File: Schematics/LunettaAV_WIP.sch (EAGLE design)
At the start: 98 parts, among them IC1 TLC339P, IC10 40106N, IC2 4046N, IC3 7809\, IC4 4040N, IC5 7805, IC6 4017N, IC7 4051N, IC8 4094N, J1 POWER_JACKPOWER_JACK_SLOT, U1 LM358, U3 LM358

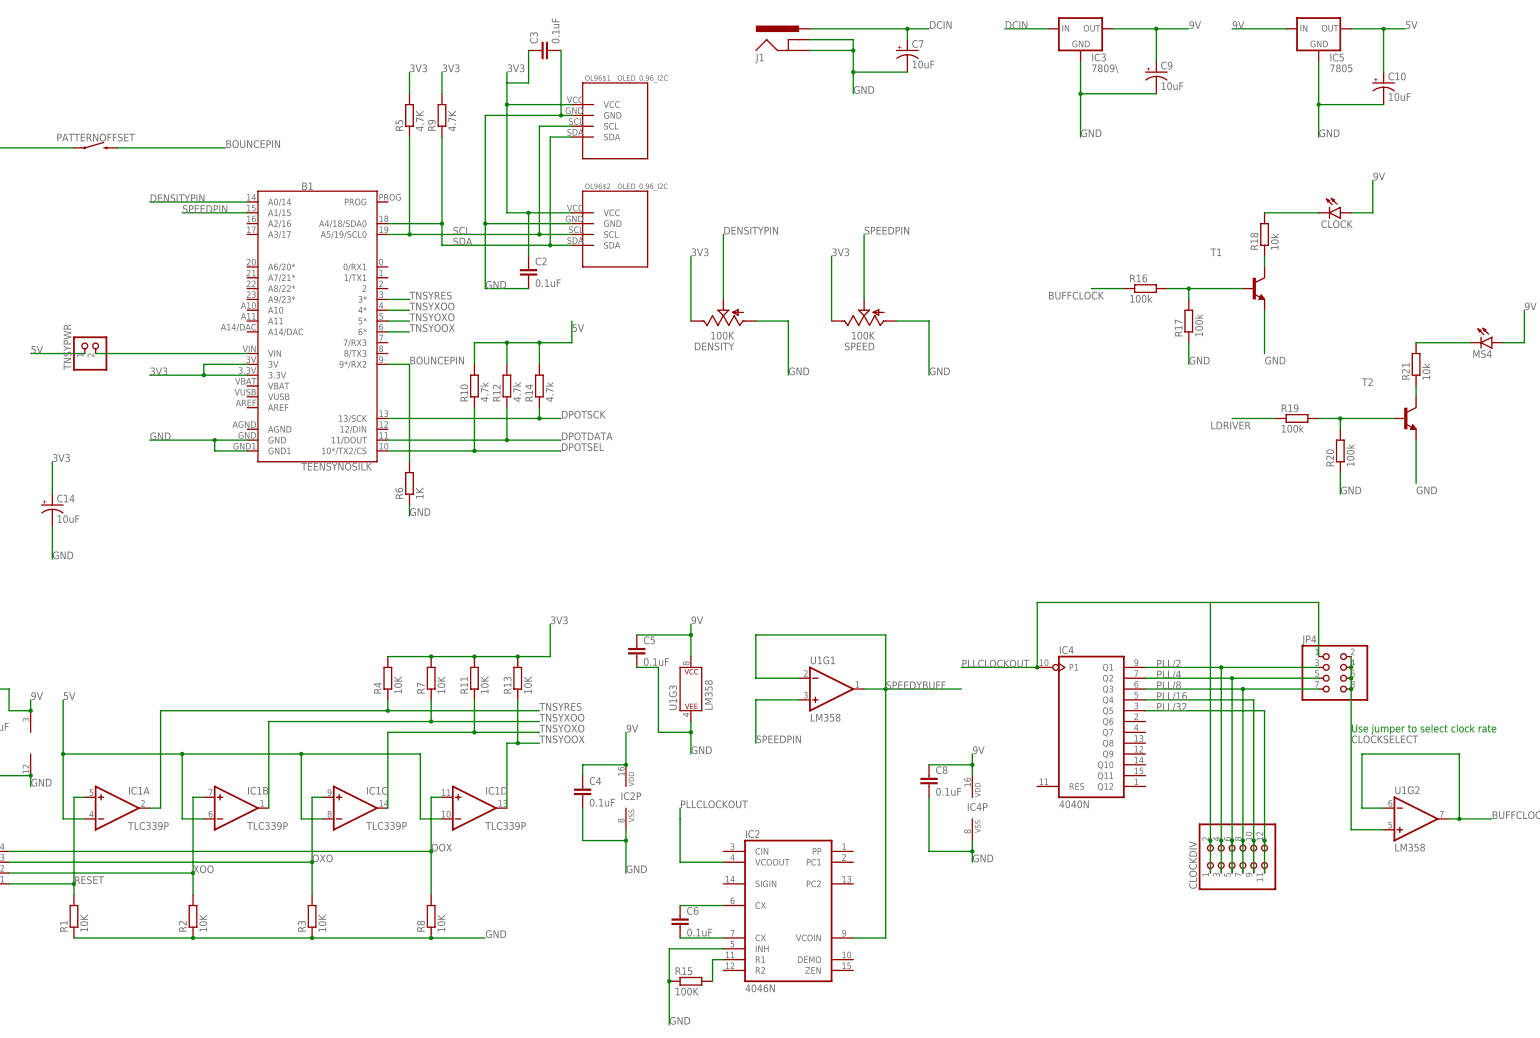
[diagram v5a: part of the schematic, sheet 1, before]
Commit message: fix minor schematic issues for a cleaner bom
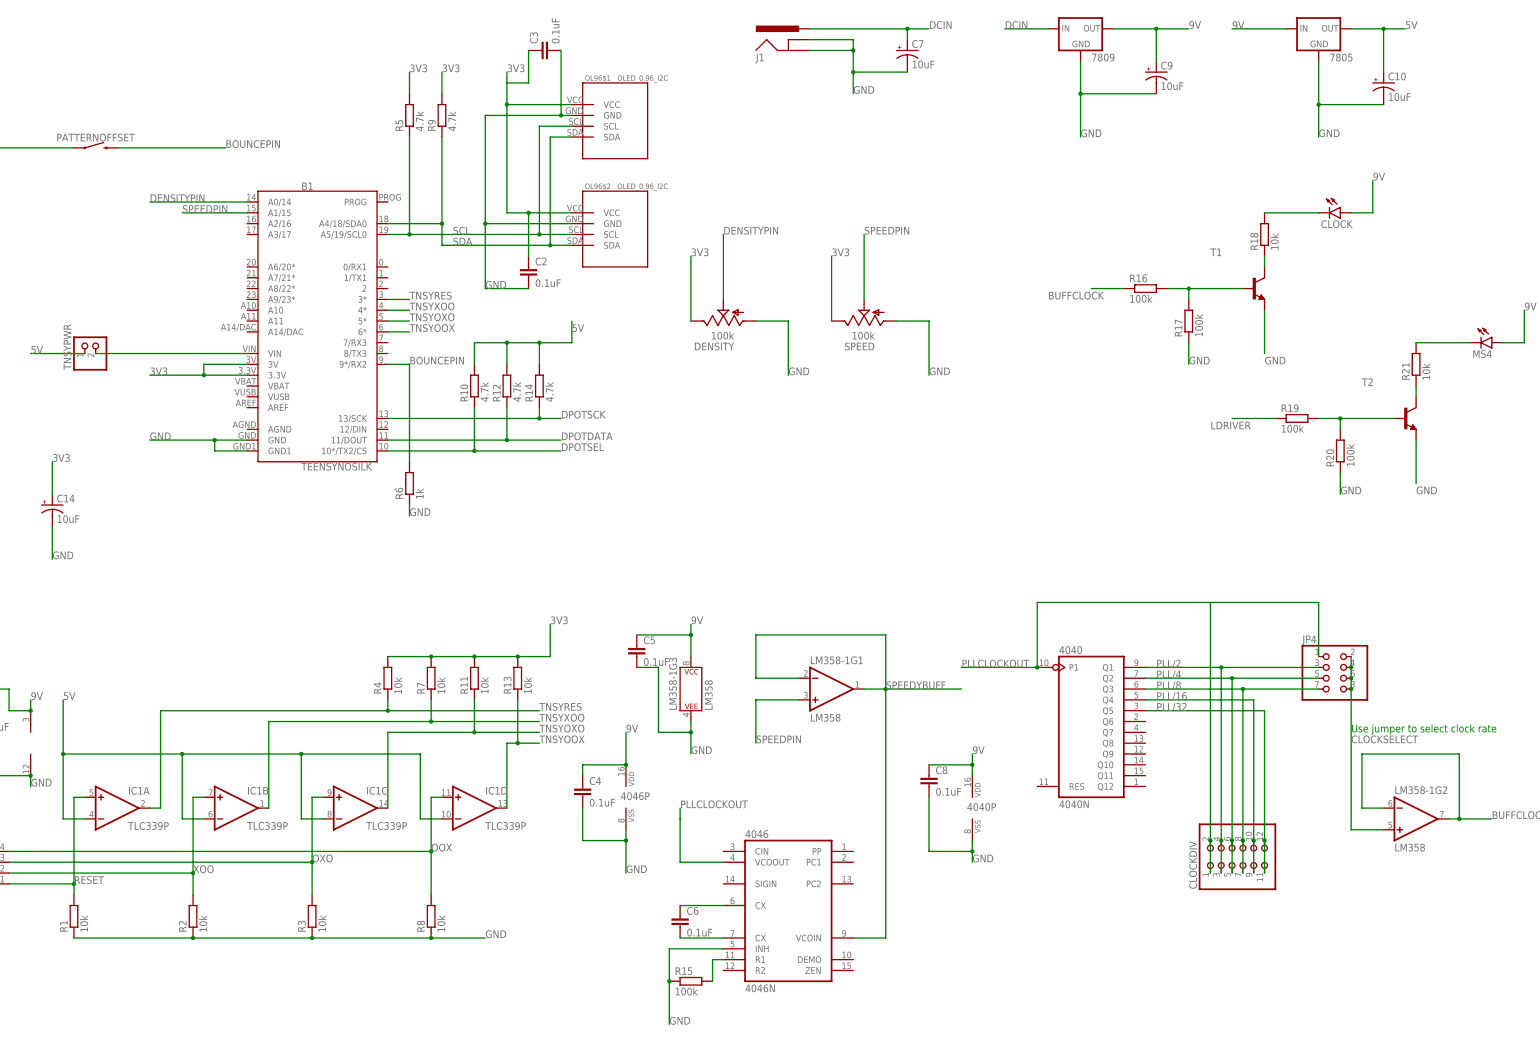
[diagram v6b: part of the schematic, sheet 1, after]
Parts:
- 7809: value 7809\ -> 7809
- C19: value .1uF -> 1uF; device capacitor-wima:C2.5/2 -> capacitor-wima:C5/3.5
- DENSITY, FREQ, R15, SPEED: value 100K -> 100k
- MCP41050: value MICROCHIP_MCP41050-I-PMICROCHIP_MCP41050-I-P_0_0 -> MCP41050
- R1, R11, R13, R2, R23, R24, R25, R3, R4, R7, R8: value 10K -> 10k
- R22, R26, R6: value 1K -> 1k
- R5, R9: value 4.7K -> 4.7k
- renumbered IC10 to 40106, IC2 to 4046, IC3 to 7809, IC4 to 4040, IC5 to 7805, IC6 to 4017, IC7 to 4051, IC8 to 4094, U1 to LM358-1, U3 to LM358-2

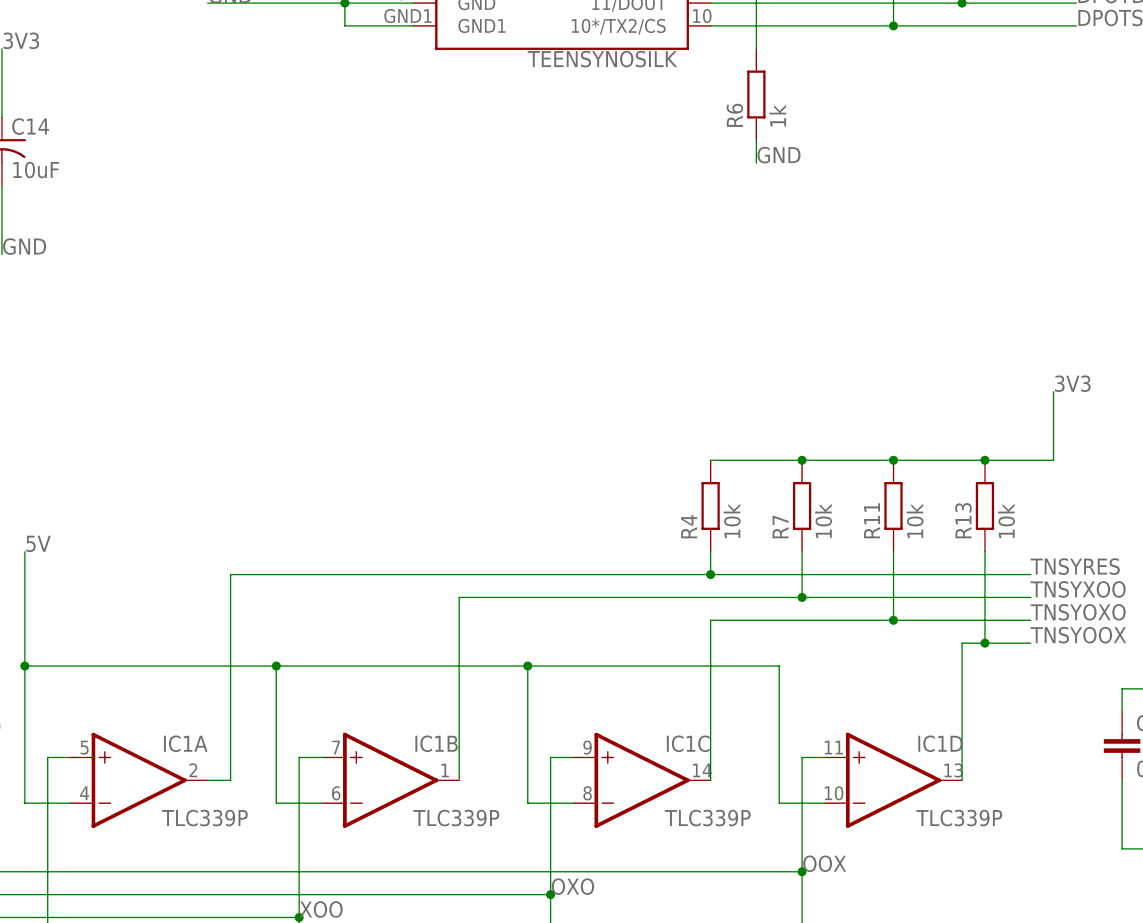
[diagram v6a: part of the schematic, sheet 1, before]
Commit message: redesign board for mounting holes
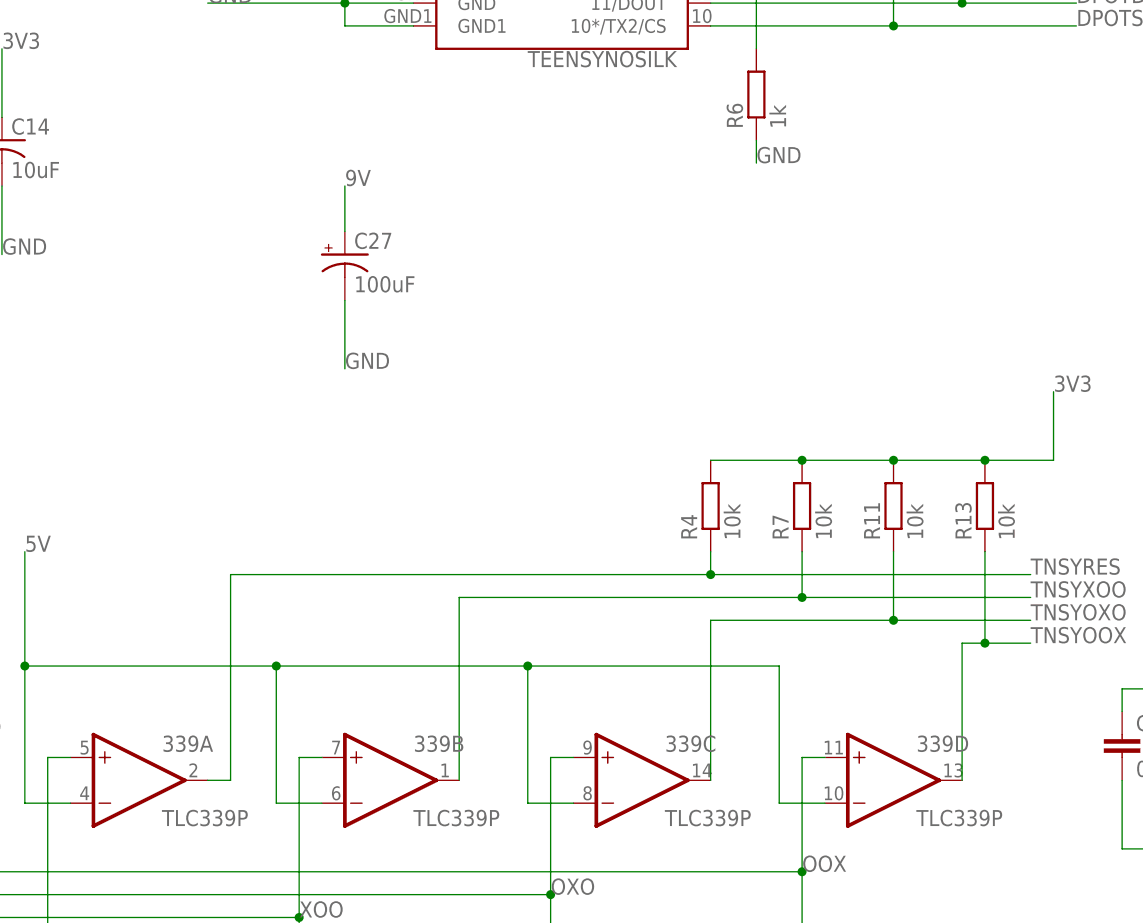
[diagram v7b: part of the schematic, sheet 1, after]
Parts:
- added C27: 100uF, SparkFun-Capacitors:100UF-POLAR-RADIAL-2.5MM-25V-20%
- renumbered IC1 to 339
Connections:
- net 9V: now also C27.+
- net GND: now also C27.-
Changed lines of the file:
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@@
 <part name="ERASE" library="SparkFun-Switches" deviceset="MOMENTARY-SWITCH-SPST" device="-PTH-12MM" value=""/>
 <part name="PATTERNOFFSET" library="SparkFun-Switches" deviceset="MOMENTARY-SWITCH-SPST" device="-PTH-12MM" value=""/>
-<part name="IC1" library="linear" library_urn="urn:adsk.eagle:library:262" deviceset="TLC339" device="P" package3d_urn="urn:adsk.eagle:package:16407/2"/>
+<part name="339" library="linear" library_urn="urn:adsk.eagle:library:262" deviceset="TLC339" device="P" package3d_urn="urn:adsk.eagle:package:16407/2"/>
 <part name="R4" library="MusicThingModular" deviceset="RESISTOR" device="7MM" value="10k"/>
 <part name="R7" library="MusicThingModular" deviceset="RESISTOR" device="7MM" value="10k"/>
@@
 <part name="TNSYSELECT" library="jumper" library_urn="urn:adsk.eagle:library:252" deviceset="JP4E" device="" package3d_urn="urn:adsk.eagle:package:15463/1"/>
 <part name="C14" library="SparkFun-Capacitors" deviceset="10UF-POLAR" device="-RADIAL-2.5MM-25V-20%" value="10uF"/>
+<part name="C27" library="SparkFun-Capacitors" deviceset="100UF-POLAR" device="-RADIAL-2.5MM-25V-20%" value="100uF"/>
 </parts>
 <sheets>
@@
 <attribute name="VALUE" x="-106.68" y="141.732" size="1.778" layer="96" font="vector" align="top-center"/>
 </instance>
-<instance part="IC1" gate="A" x="-101.6" y="-12.7" smashed="yes">
+<instance part="339" gate="A" x="-101.6" y="-12.7" smashed="yes">
 <attribute name="NAME" x="-99.06" y="-9.525" size="1.778" layer="95"/>
 <attribute name="VALUE" x="-99.06" y="-17.78" size="1.778" layer="96"/>
 </instance>
-<instance part="IC1" gate="B" x="-73.66" y="-12.7" smashed="yes">
+<instance part="339" gate="B" x="-73.66" y="-12.7" smashed="yes">
 <attribute name="NAME" x="-71.12" y="-9.525" size="1.778" layer="95"/>
 <attribute name="VALUE" x="-71.12" y="-17.78" size="1.778" layer="96"/>
 </instance>
-<instance part="IC1" gate="C" x="-45.72" y="-12.7" smashed="yes">
+<instance part="339" gate="C" x="-45.72" y="-12.7" smashed="yes">
 <attribute name="NAME" x="-43.18" y="-9.525" size="1.778" layer="95"/>
 <attribute name="VALUE" x="-43.18" y="-17.78" size="1.778" layer="96"/>
 </instance>
-<instance part="IC1" gate="D" x="-17.78" y="-12.7" smashed="yes">
+<instance part="339" gate="D" x="-17.78" y="-12.7" smashed="yes">
 <attribute name="NAME" x="-15.24" y="-9.525" size="1.778" layer="95"/>
 <attribute name="VALUE" x="-15.24" y="-17.78" size="1.778" layer="96"/>
 </instance>
-<instance part="IC1" gate="P" x="-121.92" y="2.54" smashed="yes"/>
+<instance part="339" gate="P" x="-121.92" y="2.54" smashed="yes"/>
 <instance part="R4" gate="G$1" x="-38.1" y="17.78" smashed="yes" rot="R90">
 <attribute name="NAME" x="-39.5986" y="13.97" size="1.778" layer="95" rot="R90"/>
@@
 <attribute name="NAME" x="-115.824" y="59.055" size="1.778" layer="95" font="vector"/>
 <attribute name="VALUE" x="-115.824" y="54.229" size="1.778" layer="96" font="vector"/>
+</instance>
+<instance part="C27" gate="G$1" x="-78.74" y="45.72" smashed="yes">
+<attribute name="NAME" x="-77.724" y="46.355" size="1.778" layer="95" font="vector"/>
+<attribute name="VALUE" x="-77.724" y="41.529" size="1.778" layer="96" font="vector"/>
 </instance>
 </instances>
@@
 </segment>
 <segment>
-<pinref part="IC1" gate="P" pin="V-"/>
+<pinref part="339" gate="P" pin="V-"/>
 <wire x1="-121.92" y1="-5.08" x2="-121.92" y2="-7.62" width="0.1524" layer="91"/>
 <label x="-121.92" y="-7.62" size="1.778" layer="95"/>
@@
 <wire x1="-116.84" y1="53.34" x2="-116.84" y2="45.72" width="0.1524" layer="91"/>
 <label x="-116.84" y="45.72" size="1.778" layer="95"/>
+</segment>
+<segment>
+<pinref part="C27" gate="G$1" pin="-"/>
+<wire x1="-78.74" y1="40.64" x2="-78.74" y2="33.02" width="0.1524" layer="91"/>
+<label x="-78.74" y="33.02" size="1.778" layer="95"/>
 </segment>
 </net>
@@
 <wire x1="-114.3" y1="0" x2="-114.3" y2="-15.24" width="0.1524" layer="91"/>
 <junction x="-114.3" y="0"/>
-<pinref part="IC1" gate="A" pin="-IN"/>
+<pinref part="339" gate="A" pin="-IN"/>
 <wire x1="-114.3" y1="-15.24" x2="-109.22" y2="-15.24" width="0.1524" layer="91"/>
-<pinref part="IC1" gate="B" pin="-IN"/>
+<pinref part="339" gate="B" pin="-IN"/>
 <wire x1="-81.28" y1="-15.24" x2="-86.36" y2="-15.24" width="0.1524" layer="91"/>
 <wire x1="-86.36" y1="-15.24" x2="-86.36" y2="0" width="0.1524" layer="91"/>
 <junction x="-86.36" y="0"/>
-<pinref part="IC1" gate="C" pin="-IN"/>
+<pinref part="339" gate="C" pin="-IN"/>
 <wire x1="-53.34" y1="-15.24" x2="-58.42" y2="-15.24" width="0.1524" layer="91"/>
 <wire x1="-58.42" y1="-15.24" x2="-58.42" y2="0" width="0.1524" layer="91"/>
 <junction x="-58.42" y="0"/>
-<pinref part="IC1" gate="D" pin="-IN"/>
+<pinref part="339" gate="D" pin="-IN"/>
 <wire x1="-25.4" y1="-15.24" x2="-30.48" y2="-15.24" width="0.1524" layer="91"/>
 <wire x1="-30.48" y1="-15.24" x2="-30.48" y2="0" width="0.1524" layer="91"/>
@@
 </segment>
 <segment>
-<pinref part="IC1" gate="A" pin="OUT"/>
+<pinref part="339" gate="A" pin="OUT"/>
 <wire x1="-93.98" y1="-12.7" x2="-91.44" y2="-12.7" width="0.1524" layer="91"/>
 <wire x1="-91.44" y1="-12.7" x2="-91.44" y2="10.16" width="0.1524" layer="91"/>
@@
 </segment>
 <segment>
-<pinref part="IC1" gate="B" pin="OUT"/>
+<pinref part="339" gate="B" pin="OUT"/>
 <wire x1="-66.04" y1="-12.7" x2="-66.04" y2="7.62" width="0.1524" layer="91"/>
 <wire x1="-66.04" y1="7.62" x2="-27.94" y2="7.62" width="0.1524" layer="91"/>
@@
 </segment>
 <segment>
-<pinref part="IC1" gate="C" pin="OUT"/>
+<pinref part="339" gate="C" pin="OUT"/>
 <wire x1="-38.1" y1="-12.7" x2="-38.1" y2="5.08" width="0.1524" layer="91"/>
 <wire x1="-38.1" y1="5.08" x2="-17.78" y2="5.08" width="0.1524" layer="91"/>
@@
 </segment>
 <segment>
-<pinref part="IC1" gate="D" pin="OUT"/>
+<pinref part="339" gate="D" pin="OUT"/>
 <wire x1="-10.16" y1="-12.7" x2="-10.16" y2="2.54" width="0.1524" layer="91"/>
 <wire x1="-10.16" y1="2.54" x2="-7.62" y2="2.54" width="0.1524" layer="91"/>
@@
 <net name="9V" class="1">
 <segment>
-<pinref part="IC1" gate="P" pin="V+"/>
+<pinref part="339" gate="P" pin="V+"/>
 <wire x1="-121.92" y1="10.16" x2="-121.92" y2="12.7" width="0.1524" layer="91"/>
 <label x="-121.92" y="12.7" size="1.778" layer="95"/>
@@
 <label x="228.6" y="104.14" size="1.778" layer="95"/>
 </segment>
+<segment>
+<pinref part="C27" gate="G$1" pin="+"/>
+<wire x1="-78.74" y1="48.26" x2="-78.74" y2="53.34" width="0.1524" layer="91"/>
+<label x="-78.74" y="53.34" size="1.778" layer="95"/>
+</segment>
 </net>
 <net name="RESET" class="0">
@@
 <wire x1="-111.76" y1="-33.02" x2="-111.76" y2="-30.48" width="0.1524" layer="91"/>
 <label x="-111.76" y="-30.48" size="1.778" layer="95"/>
-<pinref part="IC1" gate="A" pin="+IN"/>
+<pinref part="339" gate="A" pin="+IN"/>
 <wire x1="-111.76" y1="-30.48" x2="-111.76" y2="-10.16" width="0.1524" layer="91"/>
 <wire x1="-111.76" y1="-10.16" x2="-109.22" y2="-10.16" width="0.1524" layer="91"/>
@@
 <segment>
 <label x="-83.82" y="-27.94" size="1.778" layer="95"/>
-<pinref part="IC1" gate="B" pin="+IN"/>
+<pinref part="339" gate="B" pin="+IN"/>
 <wire x1="-81.28" y1="-10.16" x2="-83.82" y2="-10.16" width="0.1524" layer="91"/>
 <wire x1="-83.82" y1="-10.16" x2="-83.82" y2="-27.94" width="0.1524" layer="91"/>
@@
 <label x="-55.88" y="-25.4" size="1.778" layer="95"/>
 <wire x1="-55.88" y1="-33.02" x2="-55.88" y2="-25.4" width="0.1524" layer="91"/>
-<pinref part="IC1" gate="C" pin="+IN"/>
+<pinref part="339" gate="C" pin="+IN"/>
 <wire x1="-55.88" y1="-25.4" x2="-55.88" y2="-10.16" width="0.1524" layer="91"/>
 <wire x1="-55.88" y1="-10.16" x2="-53.34" y2="-10.16" width="0.1524" layer="91"/>
@@
 <label x="-27.94" y="-22.86" size="1.778" layer="95"/>
 <wire x1="-27.94" y1="-33.02" x2="-27.94" y2="-22.86" width="0.1524" layer="91"/>
-<pinref part="IC1" gate="D" pin="+IN"/>
+<pinref part="339" gate="D" pin="+IN"/>
 <wire x1="-27.94" y1="-22.86" x2="-27.94" y2="-10.16" width="0.1524" layer="91"/>
 <wire x1="-27.94" y1="-10.16" x2="-25.4" y2="-10.16" width="0.1524" layer="91"/>
@@
 </segment>
 </net>
-<net name="MELODYOUT" class="0">
+<net name="MELODYOUT" class="3">
 <segment>
 <pinref part="4017" gate="A" pin="Q0"/>
@@
 </segment>
 </net>
-<net name="BUFFMEL" class="0">
+<net name="BUFFMEL" class="3">
 <segment>
 <pinref part="LM358-2" gate="G2" pin="-IN"/>
@@
 </segment>
 </net>
-<net name="OUT" class="0">
+<net name="OUT" class="3">
 <segment>
 <pinref part="MIX" gate="G$1" pin="S"/>
@@
 </segment>
 </net>
-<net name="N$40" class="0">
+<net name="N$40" class="3">
 <segment>
 <pinref part="VR4" gate="G$1" pin="2"/>
@@
 </segment>
 </net>
-<net name="N$41" class="0">
+<net name="N$41" class="3">
 <segment>
 <pinref part="C26" gate="G$1" pin="-"/>

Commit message: more changes and gerber for ordering
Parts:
- C7: value 10uF -> 100uF; device SparkFun-Capacitors:10UF-POLAR-RADIAL-2.5MM-25V-20% -> SparkFun-Capacitors:100UF-POLAR-RADIAL-2.5MM-25V-20%
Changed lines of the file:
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@@
 <part name="C10" library="SparkFun-Capacitors" deviceset="10UF-POLAR" device="-RADIAL-2.5MM-25V-20%" value="10uF"/>
 <part name="J1" library="SparkFun-Connectors" deviceset="POWER_JACK" device="POWER_JACK_SLOT" value=""/>
-<part name="C7" library="SparkFun-Capacitors" deviceset="10UF-POLAR" device="-RADIAL-2.5MM-25V-20%" value="10uF"/>
+<part name="C7" library="SparkFun-Capacitors" deviceset="100UF-POLAR" device="-RADIAL-2.5MM-25V-20%" value="100uF"/>
 <part name="R30" library="MusicThingModular" deviceset="RESISTOR" device="7MM" value="2.2k"/>
 <part name="MIX" library="MusicThingModular" deviceset="9MM_SNAP-IN_POT" device="_" value="100k"/>
